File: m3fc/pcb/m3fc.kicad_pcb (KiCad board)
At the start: 2 copper layers, 40 x 40 mm, 0 parts

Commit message: Add first go at M3FC sch and pcb
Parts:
- added C1: 100n, agg:0402, F.Cu at (93.6, 103.8)
- added C10: 100n, agg:0402, F.Cu at (100.4, 94.4)
- added C11: 1µ, agg:0402, F.Cu at (102.4, 105.0)
- added C12: 10n, agg:0402, F.Cu at (101.2, 105.0)
- added C13: 4µ7, agg:0603, F.Cu at (104.8, 98.2)
- added C14: 33p, agg:0402, F.Cu at (98.4, 110.6)
- added C15: 33p, agg:0402, F.Cu at (100.6, 110.6)
- added C2: 10µ, agg:0603, F.Cu at (108.6, 96.8)
- added C3: 100n, agg:0402, F.Cu at (105.4, 95.4)
- added C4: 100n, agg:0402, F.Cu at (108.6, 95.4)
- added C5: 100n, agg:0402, F.Cu at (90.0, 98.0)
- added C6: 100n, agg:0402, F.Cu at (105.4, 103.0)
- added C7: 4µ7, agg:0603, F.Cu at (100.4, 90.6)
- added C8: 100n, agg:0402, F.Cu at (100.4, 92.0)
- added C9: 100n, agg:0402, F.Cu at (100.4, 93.2)
- added D1: RED, agg:0603-LED, F.Cu at (95.5, 118.5)
- added D2: YLW, agg:0603-LED, F.Cu at (100.0, 119.0)
- added D3: GRN, agg:0603-LED, F.Cu at (104.5, 118.5)
- added IC1: MCP2562, agg:DFN-8-EP-MICROCHIP, F.Cu at (90.8, 103.8)
- added IC2: ADXL345, agg:ADXL3x5, F.Cu at (107.0, 92.5)
- added IC3: MS5611-01BA03, agg:MS5611, F.Cu at (107.9, 104.1)
- added IC4: STM32F411CxUx, agg:QFN-48-EP-ST, F.Cu at (100.0, 100.0)
- added J1: EAST TOP, agg:TFML-110-02-L-D, F.Cu at (115.0, 100.0)
- added J2: WEST TOP, agg:TFML-110-02-L-D, F.Cu at (85.0, 100.0)
- added J3: EAST BOT, agg:SFML-110-02-L-D-LC, B.Cu at (115.0, 100.0)
- added J4: WEST BOT, agg:SFML-110-02-L-D-LC, B.Cu at (85.0, 100.0)
- added P1: SWD_TC, agg:TC2030-NL, F.Cu at (94.0, 92.8)
- added Q1: NFET, agg:SOT-23, F.Cu at (91.2, 108.2)
- added R1: 100, agg:0402, F.Cu at (94.2, 107.0)
- added R2: 100, agg:0402, F.Cu at (97.5, 117.0)
- added R3: 100, agg:0402, F.Cu at (100.0, 117.0)
- added R4: 100, agg:0402, F.Cu at (102.5, 117.0)
- added R5: 100, agg:0402, F.Cu at (99.4, 105.0)
- added Y1: XTAL, agg:XTAL-50x32, F.Cu at (99.5, 108.0)
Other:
- rule pad_to_mask_clearance: 0.2 -> 0

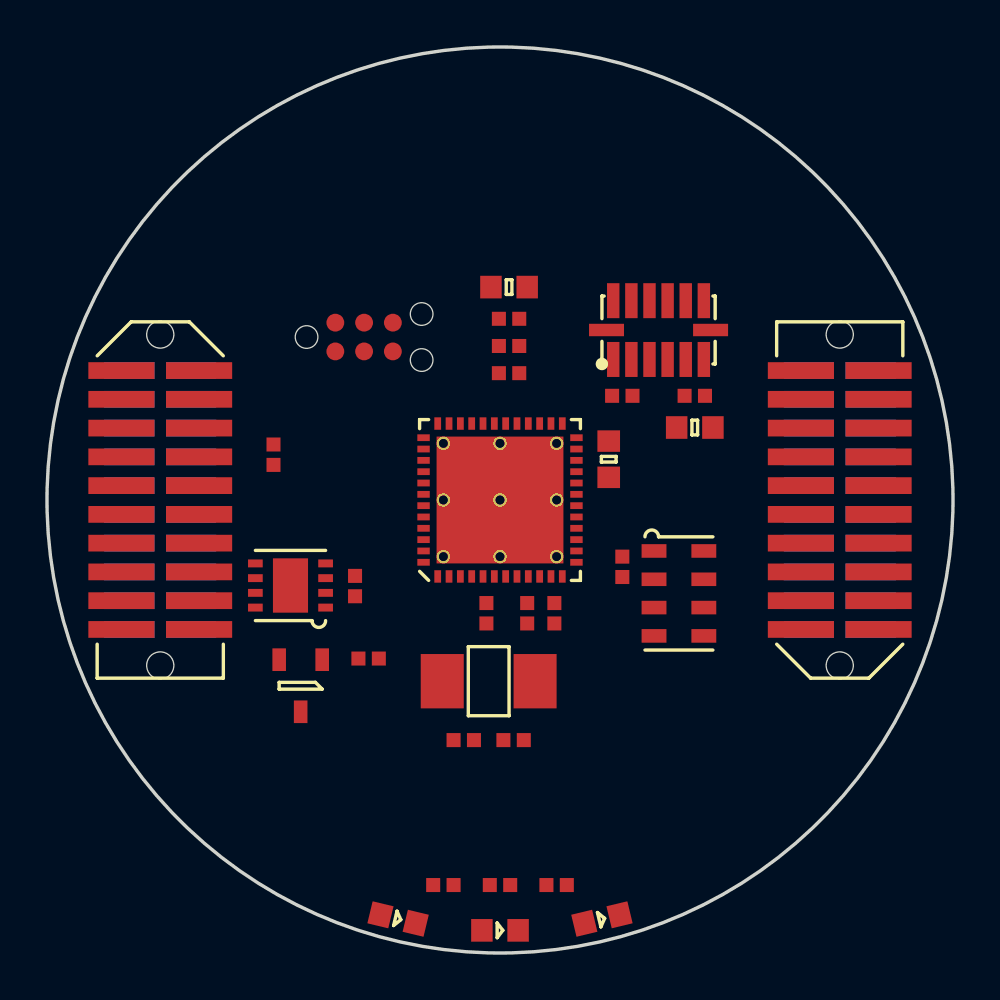
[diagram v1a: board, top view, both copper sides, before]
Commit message: Update M3FC sch with STM32F4, new xtal, new interconnect arrangement
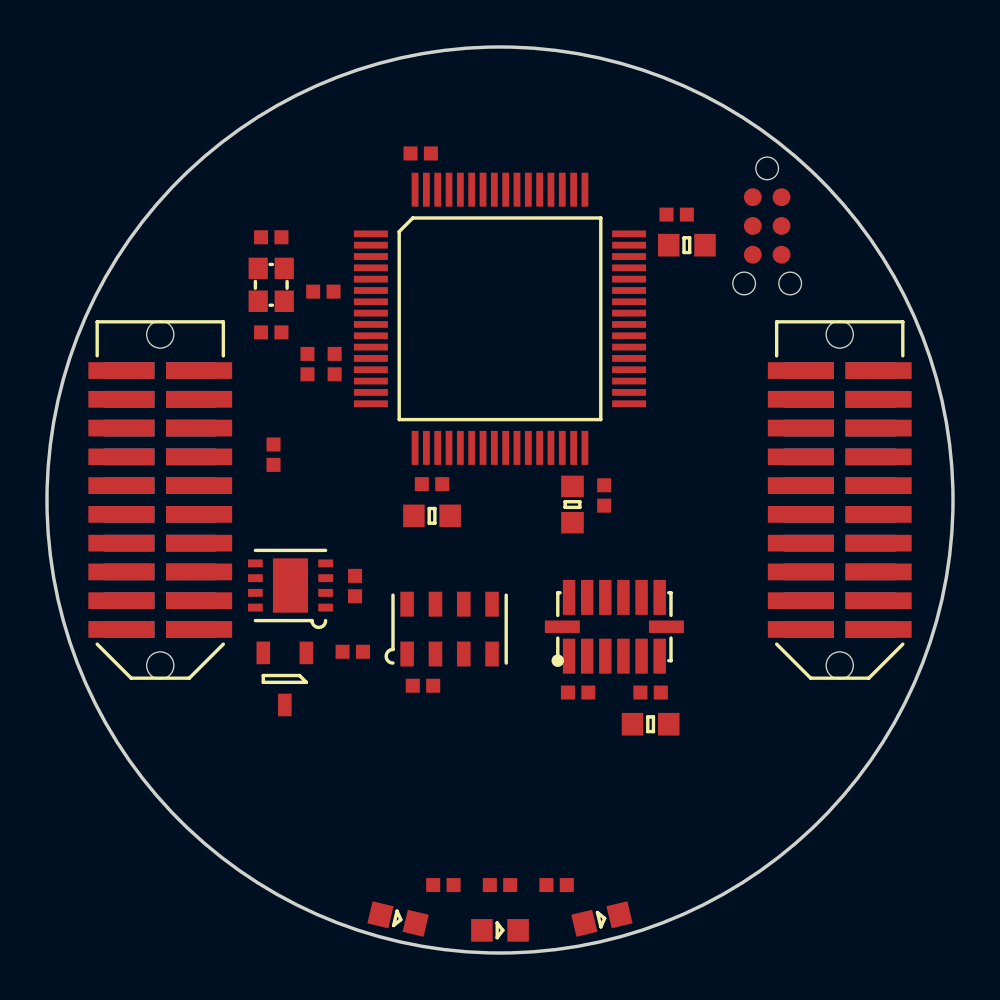
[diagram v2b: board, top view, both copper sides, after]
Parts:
- removed the C12 at (101.2, 105.0)
- removed the C13 at (104.8, 98.2)
- removed the C14 at (98.4, 110.6)
- removed the C15 at (100.6, 110.6)
- removed the IC4 at (100.0, 100.0)
- removed the J4 at (85.0, 100.0)
- added C1: 10p, agg:0402, F.Cu at (89.9, 88.4)
- added C2: 4µ7, agg:0603, F.Cu at (97.0, 100.7)
- added C3: 100n, agg:0402, F.Cu at (104.6, 99.8)
- added C4: 100n, agg:0402, F.Cu at (96.5, 84.7)
- added C5: 1µ, agg:0402, F.Cu at (91.5, 94.0)
- added C6: 10p, agg:0402, F.Cu at (89.9, 92.6)
- added IC1: STM32F405RxTx, agg:LQFP-64, F.Cu at (100.0, 92.0)
- added J1: WEST TOP, agg:TFML-110-02-L-D, F.Cu at (85.0, 100.0)
- C10: value 100n -> 2µ2; footprint agg:0402 -> agg:0603
- C11: value 1µ -> 2µ2; footprint agg:0402 -> agg:0603
- C7: value 4µ7 -> 100n; footprint agg:0603 -> agg:0402
- J2: value WEST TOP -> WEST BOT; footprint agg:TFML-110-02-L-D -> agg:SFML-110-02-L-D-LC; moved to B.Cu
- Y1: value XTAL -> 26M; footprint agg:XTAL-50x32 -> agg:XTAL-20x16
- moved Y1 20.0 mm to (89.9, 90.5)
- moved P1 18.5 mm to (111.8, 87.9), turned to 270 degrees
- moved R5 15.9 mm to (92.2, 90.8), turned to 0 degrees
- moved C13 13.2 mm to (106.7, 109.9)
- moved C14 13.2 mm to (103.5, 108.5)
- moved IC4 13.2 mm to (105.0, 105.6)
- moved C16 13.2 mm to (106.7, 108.5)
- moved C17 10.2 mm to (96.6, 108.2), turned to 0 degrees
- moved IC2 10.2 mm to (97.8, 105.7), turned to 90 degrees
- moved C10 9.67 mm to (108.2, 88.8)
- moved C7 9.34 mm to (97.0, 99.3)
- moved C8 8.71 mm to (107.8, 87.4), turned to 180 degrees
- moved C9 7.74 mm to (92.7, 94.0), turned to 270 degrees
- moved C11 4.87 mm to (103.2, 100.2)
- moved Q1 0.76 mm to (90.5, 107.9)
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- renumbered C5 to C12, C2 to C13, C3 to C14, C1 to C15, C4 to C16, C6 to C17, IC3 to IC2, IC1 to IC3, IC2 to IC4, J1 to J3, J3 to J4
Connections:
- C10 pad 1: 3v3 -> Net-(C10-Pad1)
- C11 pad 2: Net-(C11-Pad2) -> GND
- C7 pad 1: 3v3 -> GND
- C7 pad 2: GND -> 3v3
- C8 pad 1: 3v3 -> GND
- C8 pad 2: GND -> 3v3
- C9 pad 1: 3v3 -> GND
- C9 pad 2: GND -> 3v3
- J2 pad 10: /3v3_DL -> /JTCK
- J2 pad 11: /JTCK -> /3v3_DL
- J2 pad 12: /3v3_PYRO -> /RSVD1
- J2 pad 13: /JTMS -> /3v3_AUX1
- J2 pad 14: 3v3 -> /5v_CAN
- J2 pad 15: /JTDR -> /3v3_AUX2
- J2 pad 16: /3v3_RADIO -> /CAN-
- J2 pad 17: /JTDO -> /RSVD2
- J2 pad 18: /3v3_IMU -> /CAN+
- J2 pad 3: /CAN+ -> /3v3_IMU
- J2 pad 4: (no net) -> /JTDI
- J2 pad 5: /CAN- -> /3v3_RADIO
- J2 pad 6: (no net) -> /JTDR
- J2 pad 7: /5v_CAN -> 3v3
- J2 pad 8: (no net) -> /JTMS
- J2 pad 9: (no net) -> /3v3_PYRO
- R5 pad 1: Net-(C15-Pad2) -> Net-(C6-Pad1)
- Y1 pad 2: Net-(C15-Pad2) -> GND

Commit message: M3FC nearly done. D4 needs specifying.
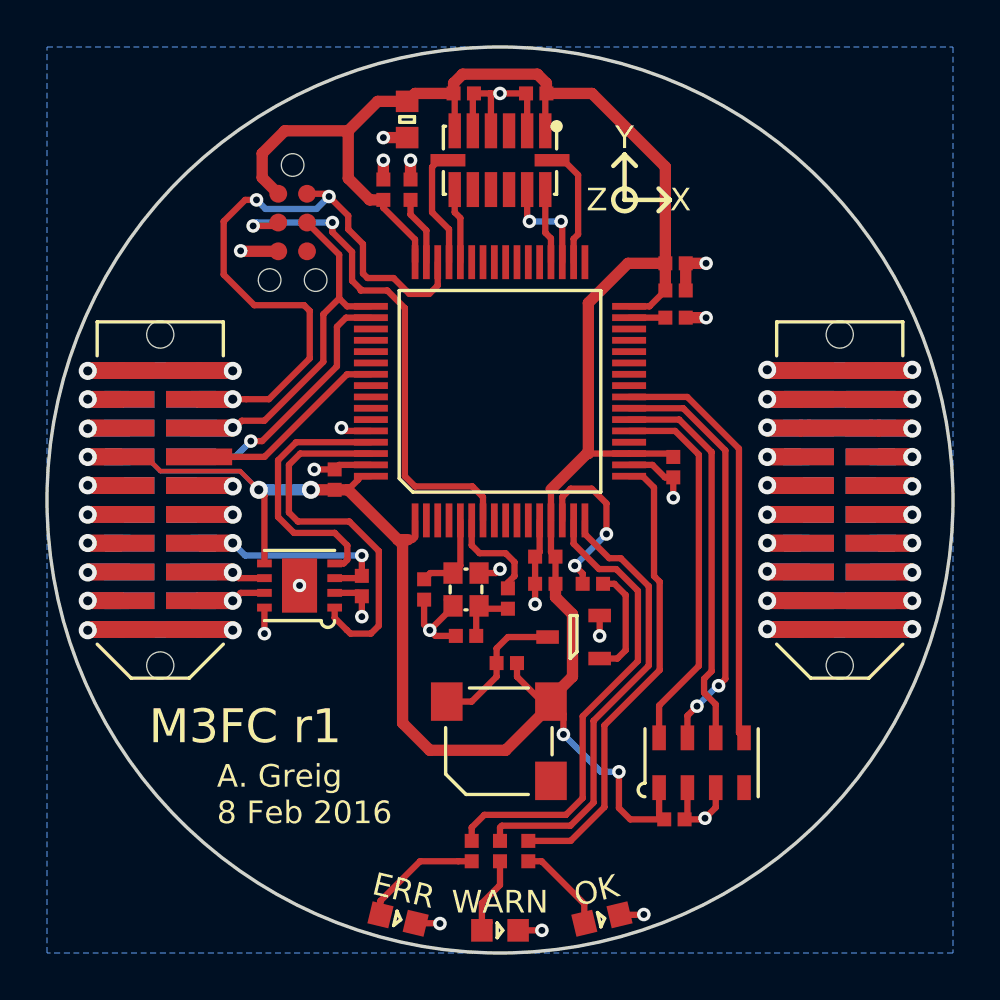
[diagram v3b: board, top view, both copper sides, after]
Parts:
- removed C12: 100n, agg:0402
- added D4: D, agg:0402, F.Cu at (100.3, 107.2)
- added LS1: SOUNDER, agg:KSSG13J12-N, F.Cu at (100.0, 110.7)
- C10, C11, C2: footprint agg:0603 -> agg:0402
- moved C13 28.8 mm to (95.9, 83.2), turned to 270 degrees
- moved C16 26.9 mm to (101.6, 82.0)
- moved C14 26.9 mm to (98.4, 82.0)
- moved IC4 21.2 mm to (100.0, 85.0), turned to 270 degrees
- moved P1 21.0 mm to (90.8, 87.8)
- moved C1 17.0 mm to (96.7, 104.0), turned to 90 degrees
- moved Y1 16.0 mm to (98.5, 104.0)
- moved C6 15.9 mm to (98.5, 106.0)
- moved R5 15.8 mm to (100.3, 104.3), turned to 90 degrees
- moved C2 15.5 mm to (107.8, 89.5), turned to 180 degrees
- moved C4 14.9 mm to (92.7, 99.1), turned to 270 degrees
- moved C5 14.3 mm to (102.0, 103.7), turned to 0 degrees
- moved C8 13.0 mm to (94.8, 86.3), turned to 270 degrees
- moved Q1 12.9 mm to (103.2, 106.0), turned to 180 degrees
- moved C9 12.6 mm to (102.0, 102.5), turned to 0 degrees
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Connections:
- IC1 pad 14: (no net) -> /BEEPER
- IC1 pad 15: (no net) -> /LED_RED
- IC1 pad 16: (no net) -> /LED_YLW
- IC1 pad 17: (no net) -> /LED_GRN
- IC1 pad 21: (no net) -> /BARO_SCLK
- IC1 pad 22: (no net) -> /BARO_SDO
- IC1 pad 23: (no net) -> /BARO_SDI
- IC1 pad 24: (no net) -> /BARO_CS
- IC1 pad 34: (no net) -> /ACCEL_SCLK
- IC1 pad 35: (no net) -> /ACCEL_SDO
- IC1 pad 36: (no net) -> /ACCEL_SDI
- IC1 pad 44: (no net) -> /ACCEL_INT
- IC1 pad 45: (no net) -> /ACCEL_CS
- IC1 pad 61: (no net) -> /CAN_RXD
- IC1 pad 62: (no net) -> /CAN_TXD
- IC2 pad 5: (no net) -> /BARO_CS
- IC2 pad 6: (no net) -> /BARO_SDO
- IC2 pad 7: (no net) -> /BARO_SDI
- IC2 pad 8: (no net) -> /BARO_SCLK
- IC3 pad 1: (no net) -> /CAN_TXD
- IC3 pad 4: (no net) -> /CAN_RXD
- IC4 pad 12: (no net) -> /ACCEL_SDO
- IC4 pad 13: (no net) -> /ACCEL_SDI
- IC4 pad 14: (no net) -> /ACCEL_SCLK
- IC4 pad 7: (no net) -> /ACCEL_CS
- IC4 pad 8: (no net) -> /ACCEL_INT
- J1 pad 10: /JTCK -> /JTDR
- J1 pad 4: /JTDO -> /JTMS
- J1 pad 6: /JTDR -> /JTCK
- J1 pad 8: /JTMS -> /JTDO
- J2 pad 10: /JTCK -> /JTDR
- J2 pad 4: /JTDI -> /JTMS
- J2 pad 6: /JTDR -> /JTCK
- J2 pad 8: /JTMS -> /JTDI
- Q1 pad 3: (no net) -> Net-(D4-Pad2)
- R1 pad 1: (no net) -> /BEEPER
- R2 pad 1: (no net) -> /LED_RED
- R3 pad 1: (no net) -> /LED_YLW
- R4 pad 1: (no net) -> /LED_GRN
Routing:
- net 3v3: track 0.00 -> 128.6 mm, vias 0 -> 5
- net GND: track 0.00 -> 94.7 mm, vias 0 -> 29
- net /JTMS: track 0.00 -> 31.7 mm, vias 0 -> 3
- net /~RST: track 0.00 -> 22.8 mm, vias 0 -> 2
- net /LED_RED: track 0.00 -> 20.9 mm
- net /LED_GRN: track 0.00 -> 20.5 mm
- net /LED_YLW: track 0.00 -> 20.1 mm
- net /BARO_CS: track 0.00 -> 18.7 mm
- net /BARO_SDI: track 0.00 -> 18.4 mm, vias 0 -> 2
- net /BARO_SDO: track 0.00 -> 17.2 mm
- net /JTCK: track 0.00 -> 17.1 mm, vias 0 -> 1
- net /BARO_SCLK: track 0.00 -> 16.7 mm
- net /CAN_TXD: track 0.00 -> 16.7 mm
- net /PYRO_SI: track 0.00 -> 12.8 mm, vias 0 -> 2
- net /PYRO_SO: track 0.00 -> 12.8 mm, vias 0 -> 2
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- added copper zone on B.Cu, net GND
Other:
- net class Default: clearance 0.2 -> 0.16; trace_width 0.25 -> 0.2
- rule trace_clearance: 0.2 -> 0.16
- rule via_min_size: 0.4 -> 0.6
- board text added: "A. Greig 8 Feb 2016"
- board text added: "ERR"
- board text added: "M3FC r1"
- board text added: "OK"
- board text added: "WARN"
- board text added: "X"
- board text added: "Y"
- board text added: "Z"

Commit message: Spec last few parts. 'Finished'.
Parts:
- D4: footprint agg:0402 -> agg:SOD-323
- moved D4 5.24 mm to (95.8, 109.8), turned to 90 degrees
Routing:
- net Net-(D4-Pad2): track 6.36 -> 7.70 mm

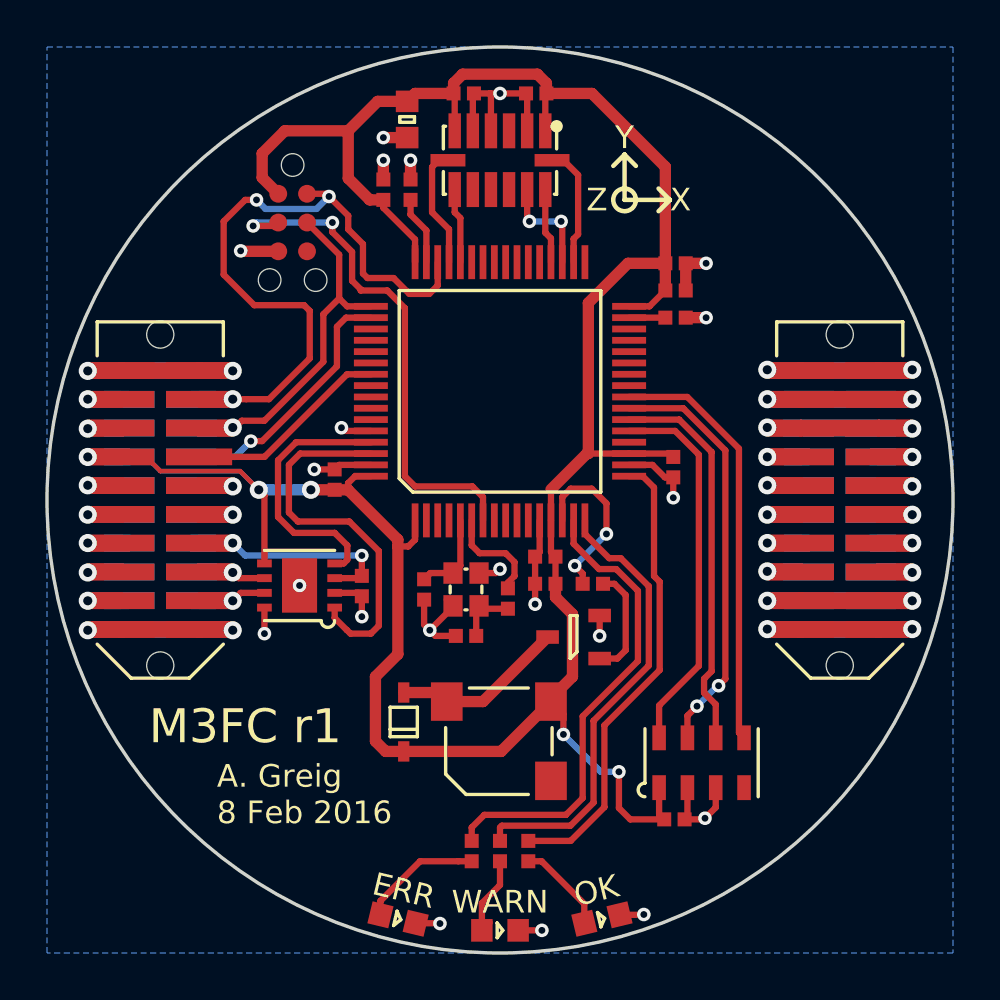
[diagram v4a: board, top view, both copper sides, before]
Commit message: add cusf logo on back silk
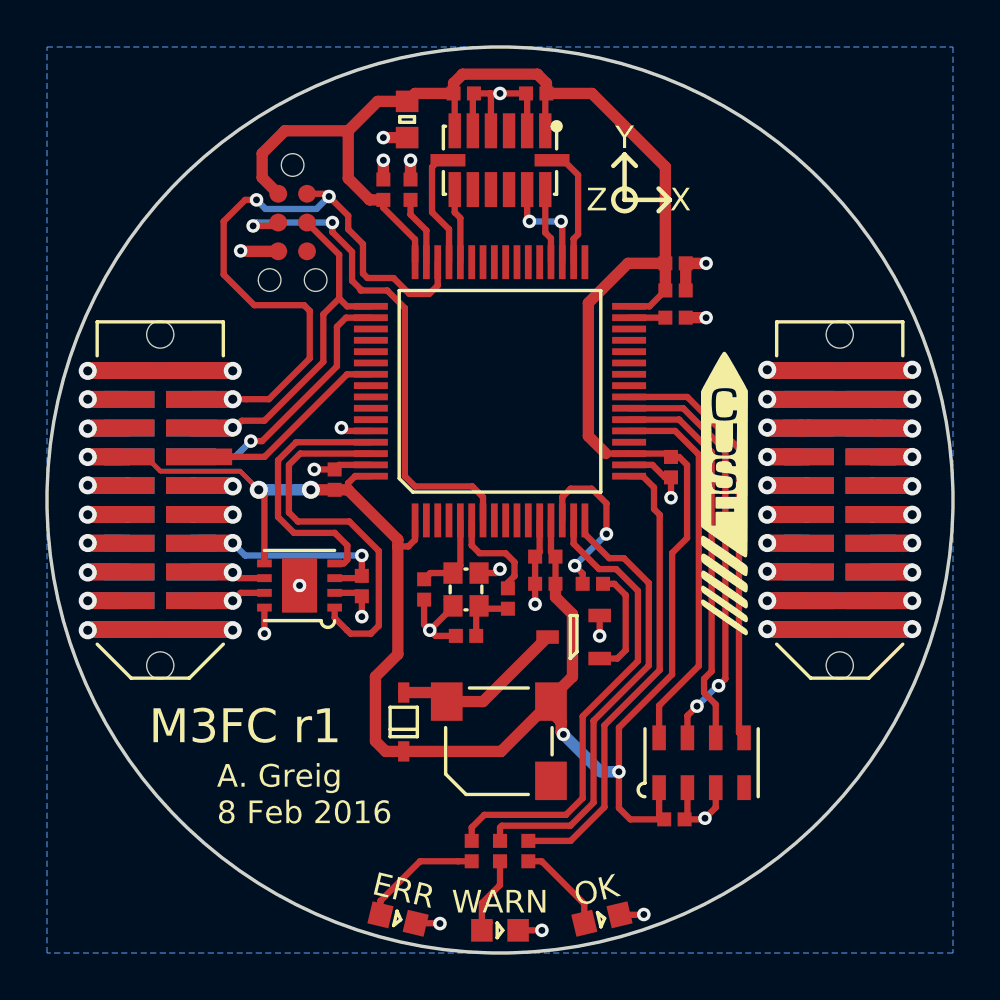
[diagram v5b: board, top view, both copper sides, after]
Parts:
- added G***: LOGO, m3fc:cusf_logo_small, F.Cu at (109.9, 99.7)
- added G***: LOGO, m3fc:cusf_logo_full, B.Cu at (100.0, 100.0)
- moved C7 0.10 mm to (107.5, 98.5)
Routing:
- net 3v3: track 128.1 -> 140.4 mm

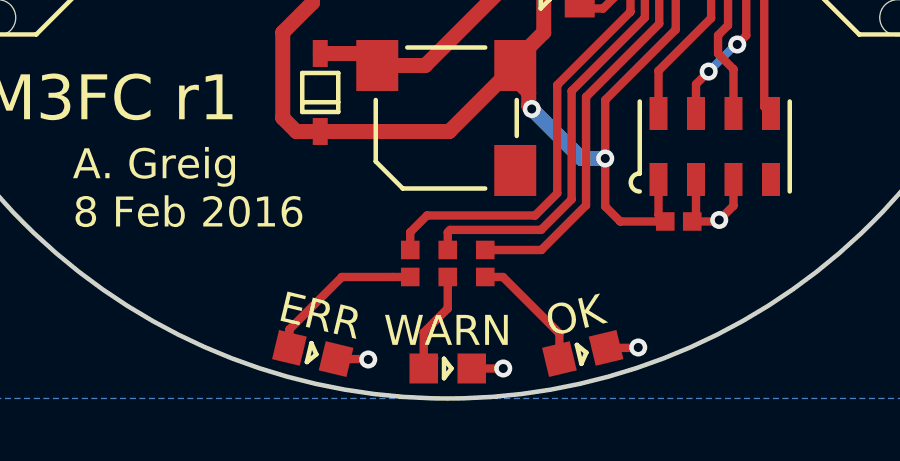
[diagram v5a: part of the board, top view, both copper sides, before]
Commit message: fix side-firing LED orientation
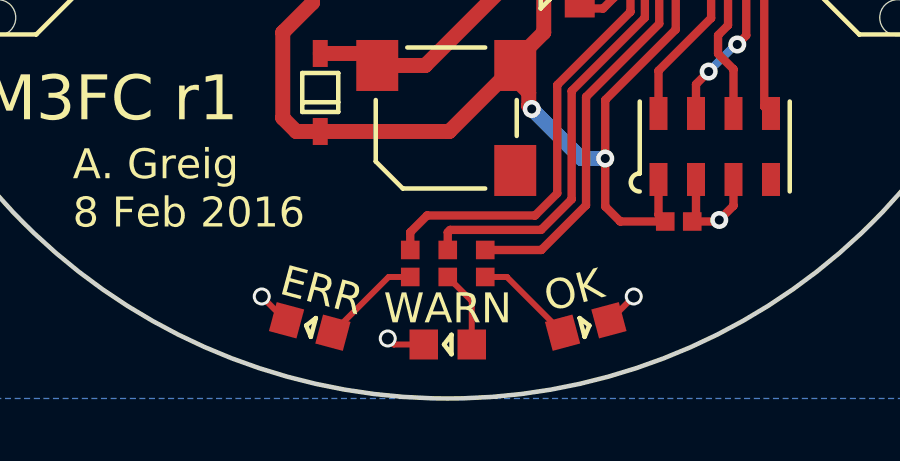
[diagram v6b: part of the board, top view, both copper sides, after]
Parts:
- moved D1 0.91 mm to (95.4, 117.6), turned to 345 degrees
- moved D3 0.91 mm to (104.6, 117.6), turned to 195 degrees
- moved D2 0.80 mm to (100.0, 118.2), turned to 0 degrees
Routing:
- net Net-(D1-Pad2): track 5.37 -> 3.35 mm
- net Net-(D2-Pad2): track 3.88 -> 2.58 mm
- net Net-(D3-Pad2): track 4.11 -> 3.35 mm
